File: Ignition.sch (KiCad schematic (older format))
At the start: 9 parts, among them Q1 Q_PMOS, Q2 Q_PMOS, Q3 Q_NMOS_SGD, Q4 Q_NMOS_SGD

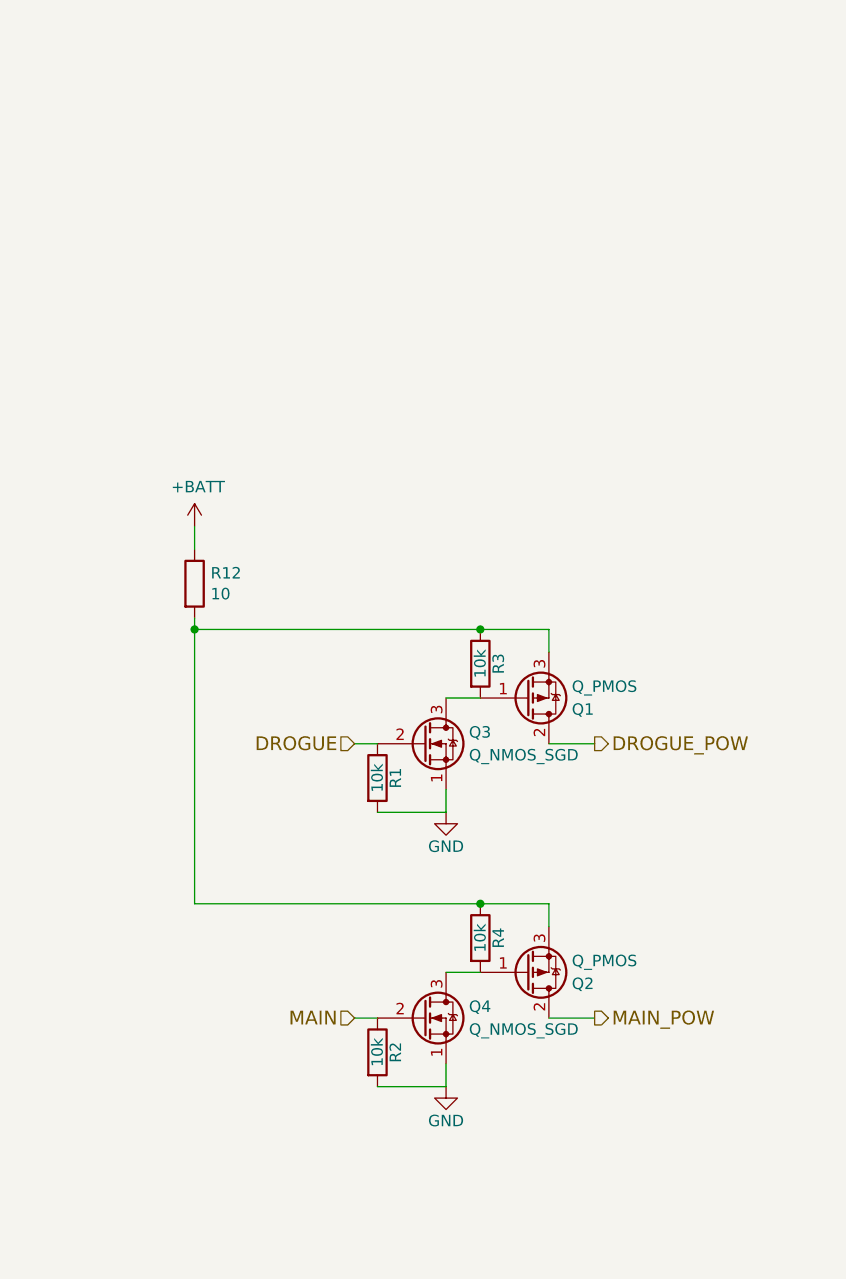
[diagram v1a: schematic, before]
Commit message: New pyro transistors New IO connector Changed SPI pins
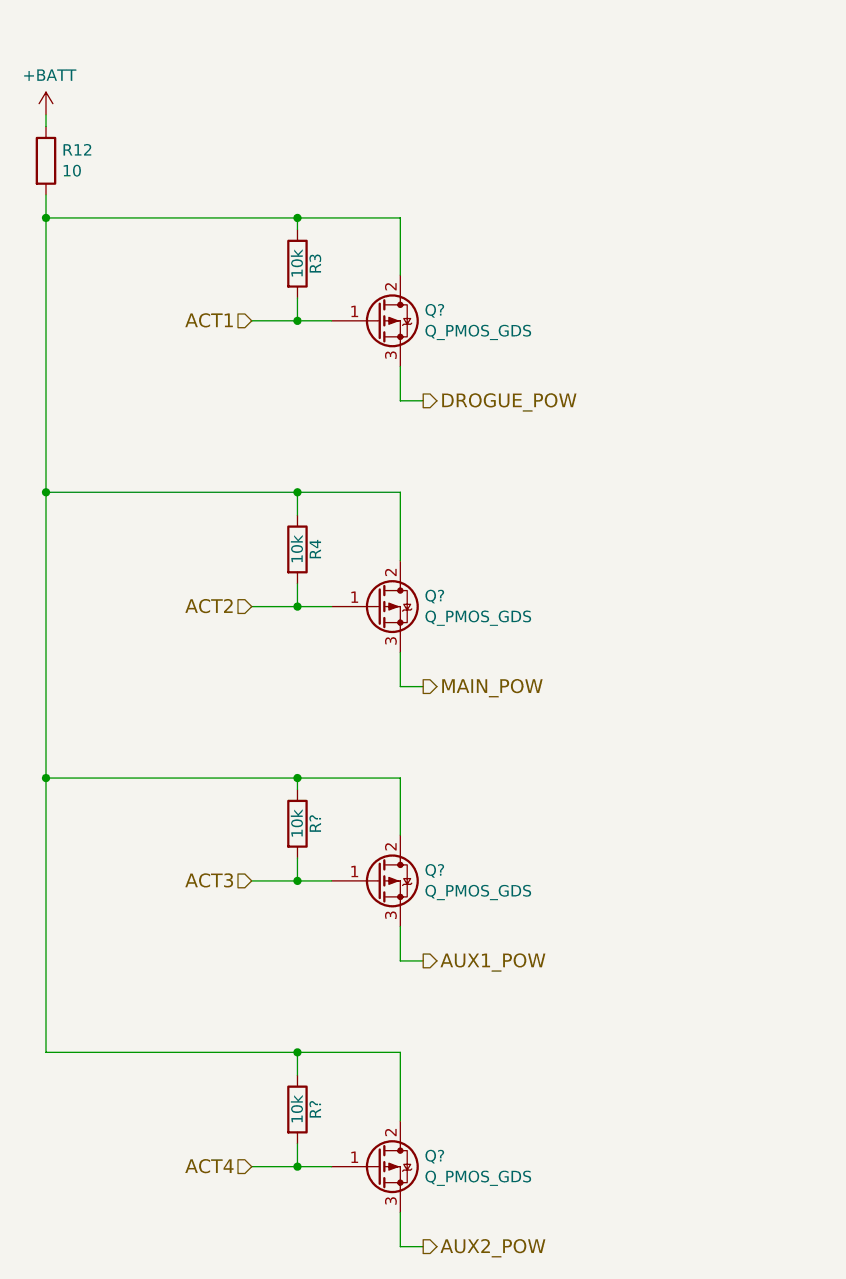
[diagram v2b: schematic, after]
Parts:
- removed Q1, Q2: Q_PMOS, Package_TO_SOT_THT:TO-220-3_Vertical, symbol Device:Q_PMOS_GDS
- removed Q3, Q4: Q_NMOS_SGD, Package_TO_SOT_THT:TO-92_Inline, symbol Device:Q_NMOS_SGD
- removed R1, R2: 10k, Resistor_THT:R_Axial_DIN0207_L6.3mm_D2.5mm_P10.16mm_Horizontal, symbol Device:R
- added Q? (x4): Q_PMOS_GDS, symbol Device:Q_PMOS_GDS
- added R? (x2): 10k, Resistor_THT:R_Axial_DIN0207_L6.3mm_D2.5mm_P10.16mm_Horizontal, symbol Device:R
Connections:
- net DROGUE_POW: now also Q?.3 (S)
- net MAIN_POW: now also Q?.3 (S)
- net ACT1: now reaches R3.2
- net ACT1: now also Q?.1 (G)
- net at R12.2, R3.1, R4.1: now also Q?.2 (D), Q?.2 (D), Q?.2 (D), Q?.2 (D), R?.1, R?.1
- net ACT2: now reaches R4.2
- net ACT2: now also Q?.1 (G)
- new net ACT3: Q?.1 (G), R?.2
- new net ACT4: Q?.1 (G), R?.2
- new net AUX1_POW: Q?.3 (S)
- new net AUX2_POW: Q?.3 (S)
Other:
- moved on the sheet: R12, R3, R4

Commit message: Starting to fix ERC errors
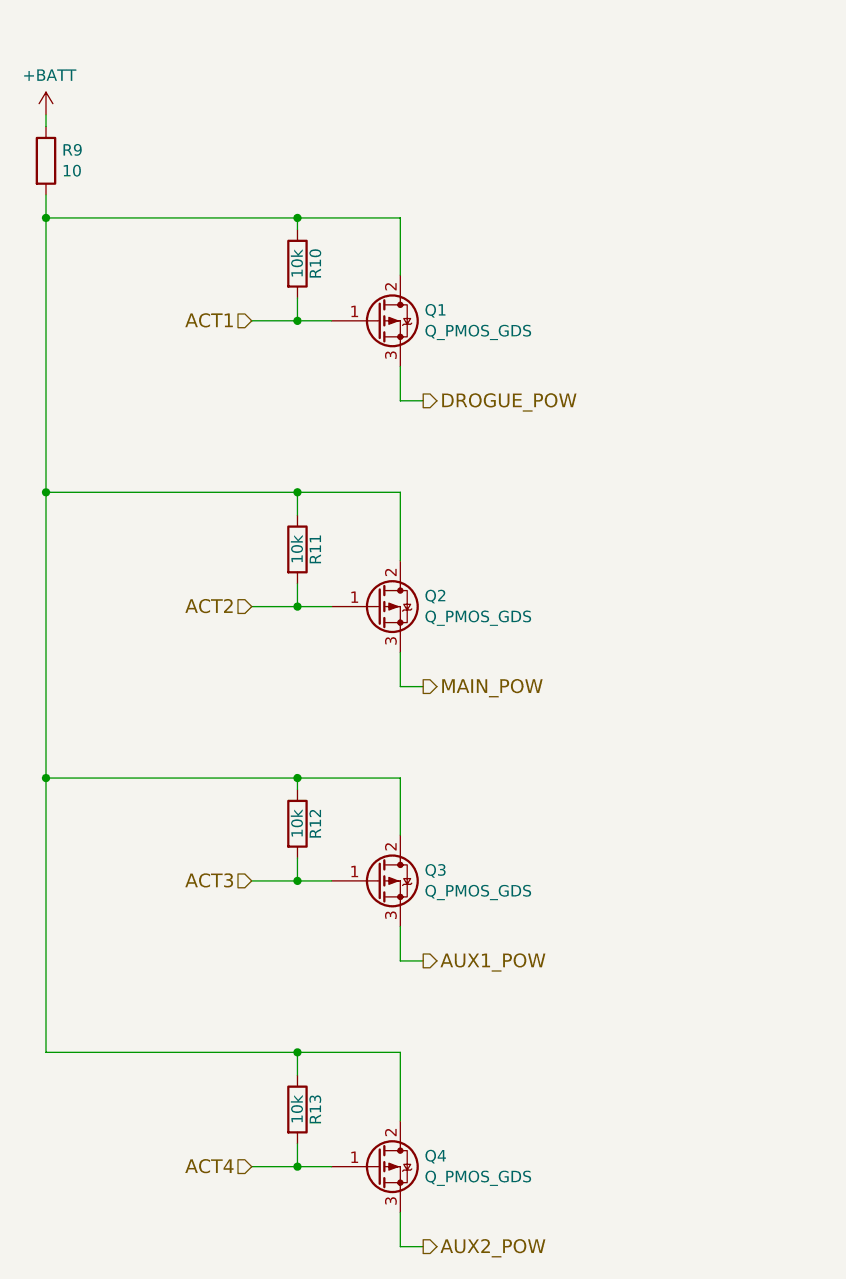
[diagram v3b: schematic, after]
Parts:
- Q1, Q2, Q3, Q4: renamed from Q?; footprint (none) -> Package_TO_SOT_SMD:SOT-23
- R10: renamed from R3; footprint Resistor_THT:R_Axial_DIN0207_L6.3mm_D2.5mm_P10.16mm_Horizontal -> Resistor_SMD:R_1206_3216Metric_Pad1.42x1.75mm_HandSolder
- R11: renamed from R4; footprint Resistor_THT:R_Axial_DIN0207_L6.3mm_D2.5mm_P10.16mm_Horizontal -> Resistor_SMD:R_1206_3216Metric_Pad1.42x1.75mm_HandSolder
- R12, R13: renamed from R?; footprint Resistor_THT:R_Axial_DIN0207_L6.3mm_D2.5mm_P10.16mm_Horizontal -> Resistor_SMD:R_1206_3216Metric_Pad1.42x1.75mm_HandSolder
- renumbered R12 to R9
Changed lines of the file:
@@
 $EndDescr
 $Comp
-L Device:R R3
+L Device:R R10
 U 1 1 5AB1848C
 P 4500 1950
-F 0 "R3" V 4580 1950 50  0000 C CNN
+F 0 "R10" V 4580 1950 50  0000 C CNN
 F 1 "10k" V 4500 1950 50  0000 C CNN
-F 2 "Resistor_THT:R_Axial_DIN0207_L6.3mm_D2.5mm_P10.16mm_Horizontal" V 4430 1950 50  0001 C CNN
+F 2 "Resistor_SMD:R_1206_3216Metric_Pad1.42x1.75mm_HandSolder" V 4430 1950 50  0001 C CNN
 F 3 "" H 4500 1950 50  0001 C CNN
 	1    4500 1950
@@
 $EndComp
 $Comp
-L Device:R R4
+L Device:R R11
 U 1 1 5AB184C4
 P 4500 3200
-F 0 "R4" V 4580 3200 50  0000 C CNN
+F 0 "R11" V 4580 3200 50  0000 C CNN
 F 1 "10k" V 4500 3200 50  0000 C CNN
-F 2 "Resistor_THT:R_Axial_DIN0207_L6.3mm_D2.5mm_P10.16mm_Horizontal" V 4430 3200 50  0001 C CNN
+F 2 "Resistor_SMD:R_1206_3216Metric_Pad1.42x1.75mm_HandSolder" V 4430 3200 50  0001 C CNN
 F 3 "" H 4500 3200 50  0001 C CNN
 	1    4500 3200
@@
 MAIN_POW
 $Comp
-L power:+BATT #PWR0122
+L power:+BATT #PWR033
 U 1 1 5C0747DE
 P 3400 1300
-F 0 "#PWR0122" H 3400 1150 50  0001 C CNN
+F 0 "#PWR033" H 3400 1150 50  0001 C CNN
 F 1 "+BATT" H 3415 1473 50  0000 C CNN
 F 2 "" H 3400 1300 50  0001 C CNN
@@
 $EndComp
 $Comp
-L Device:R R12
+L Device:R R9
 U 1 1 5C0748A3
 P 3400 1500
-F 0 "R12" H 3470 1546 50  0000 L CNN
+F 0 "R9" H 3470 1546 50  0000 L CNN
 F 1 "10" H 3470 1455 50  0000 L CNN
 F 2 "TerminalBlock:TerminalBlock_bornier-2_P5.08mm" V 3330 1500 50  0001 C CNN
@@
 	3400 1750 4500 1750
 $Comp
-L Device:Q_PMOS_GDS Q?
+L Device:Q_PMOS_GDS Q1
 U 1 1 5E75362F
 P 4850 2200
-F 0 "Q?" H 5056 2246 50  0000 L CNN
+F 0 "Q1" H 5056 2246 50  0000 L CNN
 F 1 "Q_PMOS_GDS" H 5056 2155 50  0000 L CNN
-F 2 "" H 5050 2300 50  0001 C CNN
+F 2 "Package_TO_SOT_SMD:SOT-23" H 5050 2300 50  0001 C CNN
 F 3 "~" H 4850 2200 50  0001 C CNN
 	1    4850 2200
@@
 	3400 2950 4500 2950
 $Comp
-L Device:Q_PMOS_GDS Q?
+L Device:Q_PMOS_GDS Q2
 U 1 1 5E75E62A
 P 4850 3450
-F 0 "Q?" H 5056 3496 50  0000 L CNN
+F 0 "Q2" H 5056 3496 50  0000 L CNN
 F 1 "Q_PMOS_GDS" H 5056 3405 50  0000 L CNN
-F 2 "" H 5050 3550 50  0001 C CNN
+F 2 "Package_TO_SOT_SMD:SOT-23" H 5050 3550 50  0001 C CNN
 F 3 "~" H 4850 3450 50  0001 C CNN
 	1    4850 3450
@@
 	4950 3800 5050 3800
 $Comp
-L Device:R R?
+L Device:R R12
 U 1 1 5E76AC71
 P 4500 4400
-F 0 "R?" V 4580 4400 50  0000 C CNN
+F 0 "R12" V 4580 4400 50  0000 C CNN
 F 1 "10k" V 4500 4400 50  0000 C CNN
-F 2 "Resistor_THT:R_Axial_DIN0207_L6.3mm_D2.5mm_P10.16mm_Horizontal" V 4430 4400 50  0001 C CNN
+F 2 "Resistor_SMD:R_1206_3216Metric_Pad1.42x1.75mm_HandSolder" V 4430 4400 50  0001 C CNN
 F 3 "" H 4500 4400 50  0001 C CNN
 	1    4500 4400
@@
 $EndComp
 $Comp
-L Device:R R?
+L Device:R R13
 U 1 1 5E76AC77
 P 4500 5650
-F 0 "R?" V 4580 5650 50  0000 C CNN
+F 0 "R13" V 4580 5650 50  0000 C CNN
 F 1 "10k" V 4500 5650 50  0000 C CNN
-F 2 "Resistor_THT:R_Axial_DIN0207_L6.3mm_D2.5mm_P10.16mm_Horizontal" V 4430 5650 50  0001 C CNN
+F 2 "Resistor_SMD:R_1206_3216Metric_Pad1.42x1.75mm_HandSolder" V 4430 5650 50  0001 C CNN
 F 3 "" H 4500 5650 50  0001 C CNN
 	1    4500 5650
@@
 	3400 4200 4500 4200
 $Comp
-L Device:Q_PMOS_GDS Q?
+L Device:Q_PMOS_GDS Q3
 U 1 1 5E76AC82
 P 4850 4650
-F 0 "Q?" H 5056 4696 50  0000 L CNN
+F 0 "Q3" H 5056 4696 50  0000 L CNN
 F 1 "Q_PMOS_GDS" H 5056 4605 50  0000 L CNN
-F 2 "" H 5050 4750 50  0001 C CNN
+F 2 "Package_TO_SOT_SMD:SOT-23" H 5050 4750 50  0001 C CNN
 F 3 "~" H 4850 4650 50  0001 C CNN
 	1    4850 4650
@@
 	3400 5400 4500 5400
 $Comp
-L Device:Q_PMOS_GDS Q?
+L Device:Q_PMOS_GDS Q4
 U 1 1 5E76AC93
 P 4850 5900
-F 0 "Q?" H 5056 5946 50  0000 L CNN
+F 0 "Q4" H 5056 5946 50  0000 L CNN
 F 1 "Q_PMOS_GDS" H 5056 5855 50  0000 L CNN
-F 2 "" H 5050 6000 50  0001 C CNN
+F 2 "Package_TO_SOT_SMD:SOT-23" H 5050 6000 50  0001 C CNN
 F 3 "~" H 4850 5900 50  0001 C CNN
 	1    4850 5900

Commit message: Removed redundant ADC protection diodes Basic PCB component layout
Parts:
- removed Q4: Q_PMOS_GDS, Package_TO_SOT_SMD:SOT-23, symbol Device:Q_PMOS_GDS
- removed R13: 10k, Resistor_SMD:R_1206_3216Metric_Pad1.42x1.75mm_HandSolder, symbol Device:R
- added R14, R15, R16: 5.1k, Resistor_SMD:R_1206_3216Metric_Pad1.42x1.75mm_HandSolder, symbol Device:R
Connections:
- net ACT1: now also R14.1; no longer Q1.1 (G), R10.2
- net ACT2: now also R15.1; no longer Q2.1 (G), R11.2
- net ACT3: now also R16.1; no longer Q3.1 (G), R12.2
- new net: Q1.1 (G), R10.2, R14.2
- new net: Q2.1 (G), R11.2, R15.2
- new net: Q3.1 (G), R12.2, R16.2
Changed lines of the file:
@@
 $Descr A4 11693 8268
 encoding utf-8
-Sheet 3 3
+Sheet 2 3
 Title ""
 Date ""
@@
 	1    0    0    -1
 $EndComp
-Text HLabel 4300 2200 0    60   Input ~ 0
+Text HLabel 3900 2200 0    60   Input ~ 0
 ACT1
-Text HLabel 4300 3450 0    60   Input ~ 0
+Text HLabel 3900 3450 0    60   Input ~ 0
 ACT2
 Text HLabel 5050 2550 2    60   Output ~ 0
@@
 Wire Wire Line
 	4500 2200 4650 2200
-Wire Wire Line
-	4300 2200 4500 2200
 Connection ~ 4500 2200
 Wire Wire Line
@@
 Wire Wire Line
 	4500 3450 4500 3350
-Wire Wire Line
-	4300 3450 4500 3450
 Connection ~ 4500 3450
 Wire Wire Line
@@
 	1    0    0    -1
 $EndComp
-$Comp
-L Device:R R13
-U 1 1 5E76AC77
-P 4500 5650
-F 0 "R13" V 4580 5650 50  0000 C CNN
-F 1 "10k" V 4500 5650 50  0000 C CNN
-F 2 "Resistor_SMD:R_1206_3216Metric_Pad1.42x1.75mm_HandSolder" V 4430 5650 50  0001 C CNN
-F 3 "" H 4500 5650 50  0001 C CNN
-	1    4500 5650
-	1    0    0    -1
-$EndComp
-Text HLabel 4300 4650 0    60   Input ~ 0
+Text HLabel 3900 4650 0    60   Input ~ 0
 ACT3
-Text HLabel 4300 5900 0    60   Input ~ 0
-ACT4
 Text HLabel 5050 5000 2    60   Output ~ 0
 AUX1_POW
-Text HLabel 5050 6250 2    60   Output ~ 0
-AUX2_POW
 Wire Wire Line
 	3400 4200 4500 4200
@@
 Wire Wire Line
 	4500 4650 4650 4650
-Wire Wire Line
-	4300 4650 4500 4650
 Connection ~ 4500 4650
 Wire Wire Line
@@
 Wire Wire Line
 	4950 5000 4950 4850
-Wire Wire Line
-	3400 5400 4500 5400
-$Comp
-L Device:Q_PMOS_GDS Q4
-U 1 1 5E76AC93
-P 4850 5900
-F 0 "Q4" H 5056 5946 50  0000 L CNN
-F 1 "Q_PMOS_GDS" H 5056 5855 50  0000 L CNN
-F 2 "Package_TO_SOT_SMD:SOT-23" H 5050 6000 50  0001 C CNN
-F 3 "~" H 4850 5900 50  0001 C CNN
-	1    4850 5900
-	1    0    0    -1
-$EndComp
-Wire Wire Line
-	4500 5500 4500 5400
-Connection ~ 4500 5400
-Wire Wire Line
-	4500 5400 4950 5400
-Wire Wire Line
-	4950 5400 4950 5700
-Wire Wire Line
-	4650 5900 4500 5900
-Wire Wire Line
-	4500 5900 4500 5800
-Wire Wire Line
-	4300 5900 4500 5900
-Connection ~ 4500 5900
-Wire Wire Line
-	4950 6100 4950 6250
-Wire Wire Line
-	4950 6250 5050 6250
 Wire Wire Line
 	3400 4200 3400 2950
 Connection ~ 3400 2950
-Wire Wire Line
-	3400 5400 3400 4200
-Connection ~ 3400 4200
+$Comp
+L Device:R R15
+U 1 1 5ECB6DD4
+P 4100 3450
+F 0 "R15" V 4180 3450 50  0000 C CNN
+F 1 "5.1k" V 4100 3450 50  0000 C CNN
+F 2 "Resistor_SMD:R_1206_3216Metric_Pad1.42x1.75mm_HandSolder" V 4030 3450 50  0001 C CNN
+F 3 "" H 4100 3450 50  0001 C CNN
+	1    4100 3450
+	0    -1   -1   0
+$EndComp
+$Comp
+L Device:R R14
+U 1 1 5ECB7ADD
+P 4100 2200
+F 0 "R14" V 4180 2200 50  0000 C CNN
+F 1 "5.1k" V 4100 2200 50  0000 C CNN
+F 2 "Resistor_SMD:R_1206_3216Metric_Pad1.42x1.75mm_HandSolder" V 4030 2200 50  0001 C CNN
+F 3 "" H 4100 2200 50  0001 C CNN
+	1    4100 2200
+	0    -1   -1   0
+$EndComp
+$Comp
+L Device:R R16
+U 1 1 5ECBD3A1
+P 4100 4650
+F 0 "R16" V 4180 4650 50  0000 C CNN
+F 1 "5.1k" V 4100 4650 50  0000 C CNN
+F 2 "Resistor_SMD:R_1206_3216Metric_Pad1.42x1.75mm_HandSolder" V 4030 4650 50  0001 C CNN
+F 3 "" H 4100 4650 50  0001 C CNN
+	1    4100 4650
+	0    -1   -1   0
+$EndComp
+Wire Wire Line
+	3900 4650 3950 4650
+Wire Wire Line
+	4250 4650 4500 4650
+Wire Wire Line
+	3900 3450 3950 3450
+Wire Wire Line
+	4250 3450 4500 3450
+Wire Wire Line
+	3900 2200 3950 2200
+Wire Wire Line
+	4250 2200 4500 2200
 $EndSCHEMATC

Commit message: Renamed some components?
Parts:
- renumbered R11 to R10, R12 to R11, R9 to R5, R14 to R6, R15 to R7, R16 to R8, R10 to R9
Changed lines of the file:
@@
 $EndDescr
 $Comp
-L Device:R R10
+L Device:R R9
 U 1 1 5AB1848C
 P 4500 1950
-F 0 "R10" V 4580 1950 50  0000 C CNN
+F 0 "R9" V 4580 1950 50  0000 C CNN
 F 1 "10k" V 4500 1950 50  0000 C CNN
 F 2 "Resistor_SMD:R_1206_3216Metric_Pad1.42x1.75mm_HandSolder" V 4430 1950 50  0001 C CNN
@@
 $EndComp
 $Comp
-L Device:R R11
+L Device:R R10
 U 1 1 5AB184C4
 P 4500 3200
-F 0 "R11" V 4580 3200 50  0000 C CNN
+F 0 "R10" V 4580 3200 50  0000 C CNN
 F 1 "10k" V 4500 3200 50  0000 C CNN
 F 2 "Resistor_SMD:R_1206_3216Metric_Pad1.42x1.75mm_HandSolder" V 4430 3200 50  0001 C CNN
@@
 MAIN_POW
 $Comp
-L power:+BATT #PWR033
+L power:+BATT #PWR027
 U 1 1 5C0747DE
 P 3400 1300
-F 0 "#PWR033" H 3400 1150 50  0001 C CNN
+F 0 "#PWR027" H 3400 1150 50  0001 C CNN
 F 1 "+BATT" H 3415 1473 50  0000 C CNN
 F 2 "" H 3400 1300 50  0001 C CNN
@@
 $EndComp
 $Comp
-L Device:R R9
+L Device:R R5
 U 1 1 5C0748A3
 P 3400 1500
-F 0 "R9" H 3470 1546 50  0000 L CNN
+F 0 "R5" H 3470 1546 50  0000 L CNN
 F 1 "10" H 3470 1455 50  0000 L CNN
 F 2 "TerminalBlock:TerminalBlock_bornier-2_P5.08mm" V 3330 1500 50  0001 C CNN
@@
 	4950 3800 5050 3800
 $Comp
-L Device:R R12
+L Device:R R11
 U 1 1 5E76AC71
 P 4500 4400
-F 0 "R12" V 4580 4400 50  0000 C CNN
+F 0 "R11" V 4580 4400 50  0000 C CNN
 F 1 "10k" V 4500 4400 50  0000 C CNN
 F 2 "Resistor_SMD:R_1206_3216Metric_Pad1.42x1.75mm_HandSolder" V 4430 4400 50  0001 C CNN
@@
 Connection ~ 3400 2950
 $Comp
-L Device:R R15
+L Device:R R7
 U 1 1 5ECB6DD4
 P 4100 3450
-F 0 "R15" V 4180 3450 50  0000 C CNN
+F 0 "R7" V 4180 3450 50  0000 C CNN
 F 1 "5.1k" V 4100 3450 50  0000 C CNN
 F 2 "Resistor_SMD:R_1206_3216Metric_Pad1.42x1.75mm_HandSolder" V 4030 3450 50  0001 C CNN
@@
 $EndComp
 $Comp
-L Device:R R14
+L Device:R R6
 U 1 1 5ECB7ADD
 P 4100 2200
-F 0 "R14" V 4180 2200 50  0000 C CNN
+F 0 "R6" V 4180 2200 50  0000 C CNN
 F 1 "5.1k" V 4100 2200 50  0000 C CNN
 F 2 "Resistor_SMD:R_1206_3216Metric_Pad1.42x1.75mm_HandSolder" V 4030 2200 50  0001 C CNN
@@
 $EndComp
 $Comp
-L Device:R R16
+L Device:R R8
 U 1 1 5ECBD3A1
 P 4100 4650
-F 0 "R16" V 4180 4650 50  0000 C CNN
+F 0 "R8" V 4180 4650 50  0000 C CNN
 F 1 "5.1k" V 4100 4650 50  0000 C CNN
 F 2 "Resistor_SMD:R_1206_3216Metric_Pad1.42x1.75mm_HandSolder" V 4030 4650 50  0001 C CNN
